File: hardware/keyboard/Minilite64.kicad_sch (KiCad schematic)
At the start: 129 parts, among them J1 20P 1.0mm FFC Type A, SW1 ~/`, SW10 (/9, SW11 )/0, SW12 _/-, SW13 +/=, SW14 Backspace, SW15 Tab, SW16 Q, SW17 W, SW18 E, SW19 R, SW2 !/1, SW20 T, SW21 Y, SW22 U, SW23 I, SW24 O, SW25 P, SW26 {/[, SW27 }/], SW28 |/\, SW29 Caps Lock, SW3 @/2, SW30 A, SW31 S, SW32 D, SW33 F, SW34 G, SW35 H, SW36 J, SW37 K, SW38 L, SW39 :/;, SW4 #/3, SW40 "/', SW41 Enter, SW42 Shift, SW43 Z, SW44 X, SW45 C, SW46 V, SW47 B, SW48 N, SW49 M, SW5 $/4, SW50 </,, SW51 >/., SW52 ?//, SW53 Shift, SW54 Ctrl, SW55 Win, SW56 Alt, SW57 Fn1, SW59 Fn2, SW6 %/5, SW60 Menu, SW61 Fn3, SW62 Alt, SW63 Win, SW64 Ctrl, SW7 ^/6, SW8 &/7, SW9 */8

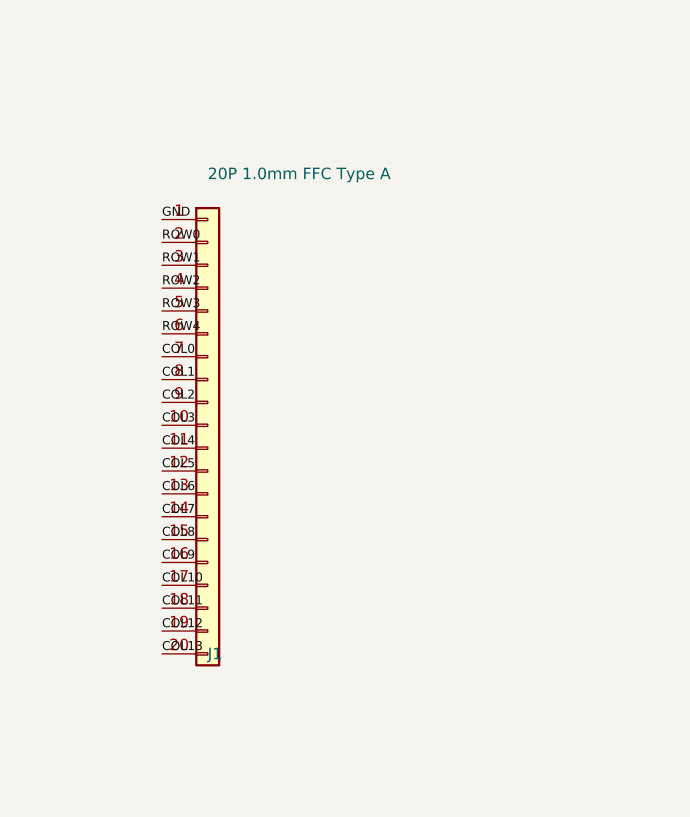
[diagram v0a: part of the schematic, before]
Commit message: Finalize FFC routing and assembly-safe hardware
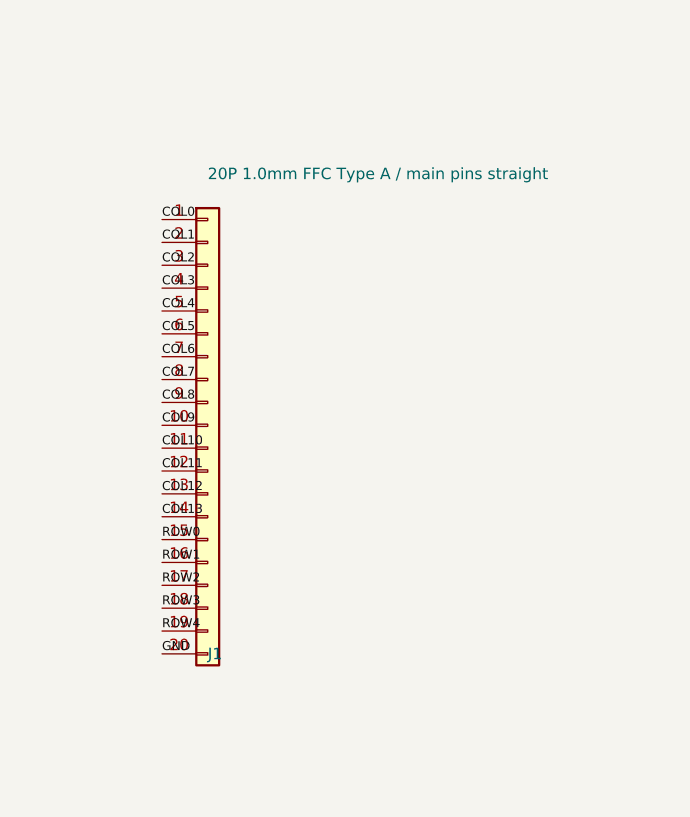
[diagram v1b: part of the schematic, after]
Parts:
- J1: value 20P 1.0mm FFC Type A -> 20P 1.0mm FFC Type A / main pins straight
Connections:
- net COL0: now also J1.1 (Pin_1); no longer J1.7 (Pin_7)
- net COL1: now also J1.2 (Pin_2); no longer J1.8 (Pin_8)
- net COL10: now also J1.11 (Pin_11); no longer J1.17 (Pin_17)
- net COL11: now also J1.12 (Pin_12); no longer J1.18 (Pin_18)
- net COL12: now also J1.13 (Pin_13); no longer J1.19 (Pin_19)
- net COL13: now also J1.14 (Pin_14); no longer J1.20 (Pin_20)
- net COL2: now also J1.3 (Pin_3); no longer J1.9 (Pin_9)
- net COL3: now also J1.4 (Pin_4); no longer J1.10 (Pin_10)
- net COL4: now also J1.5 (Pin_5); no longer J1.11 (Pin_11)
- net COL5: now also J1.6 (Pin_6); no longer J1.12 (Pin_12)
- net COL6: now also J1.7 (Pin_7); no longer J1.13 (Pin_13)
- net COL7: now also J1.8 (Pin_8); no longer J1.14 (Pin_14)
- net COL8: now also J1.9 (Pin_9); no longer J1.15 (Pin_15)
- net COL9: now also J1.10 (Pin_10); no longer J1.16 (Pin_16)
- net GND: now also J1.20 (Pin_20); no longer J1.1 (Pin_1)
- net ROW0: now also J1.15 (Pin_15); no longer J1.2 (Pin_2)
- net ROW1: now also J1.16 (Pin_16); no longer J1.3 (Pin_3)
- net ROW2: now also J1.17 (Pin_17); no longer J1.4 (Pin_4)
- net ROW3: now also J1.18 (Pin_18); no longer J1.5 (Pin_5)
- net ROW4: now also J1.19 (Pin_19); no longer J1.6 (Pin_6)
